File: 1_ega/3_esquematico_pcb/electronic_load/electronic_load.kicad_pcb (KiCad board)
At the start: 2 copper layers, 28 parts, among them J1 Encoder, J2 LCD_I2C, J3 GND, J4 MOS_GATE, J5 Isense, J6 Vload_LPF, J7 5V, Q1 IRF540N, SW1 BTN_MENU, SW2 BTN_STOP, U1 TL084

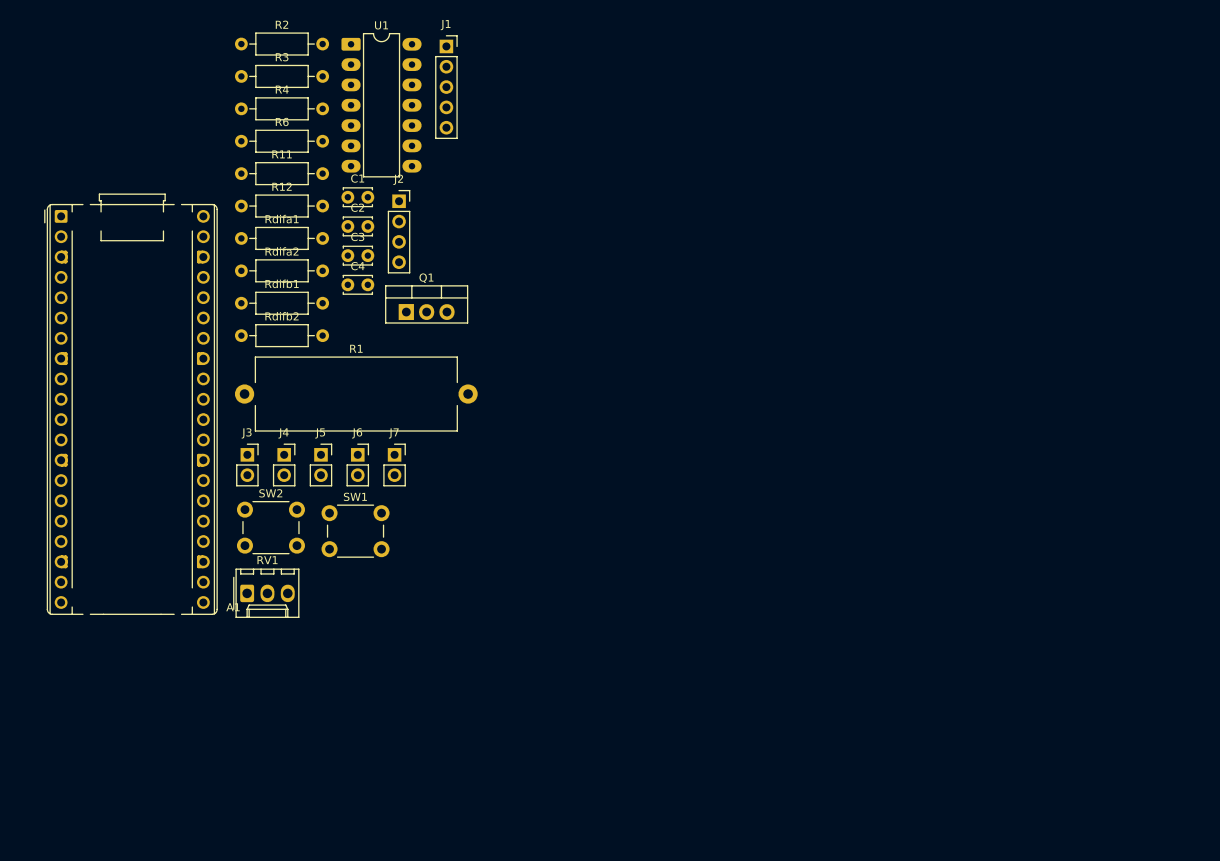
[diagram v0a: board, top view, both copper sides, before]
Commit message: test version of i2c_guard
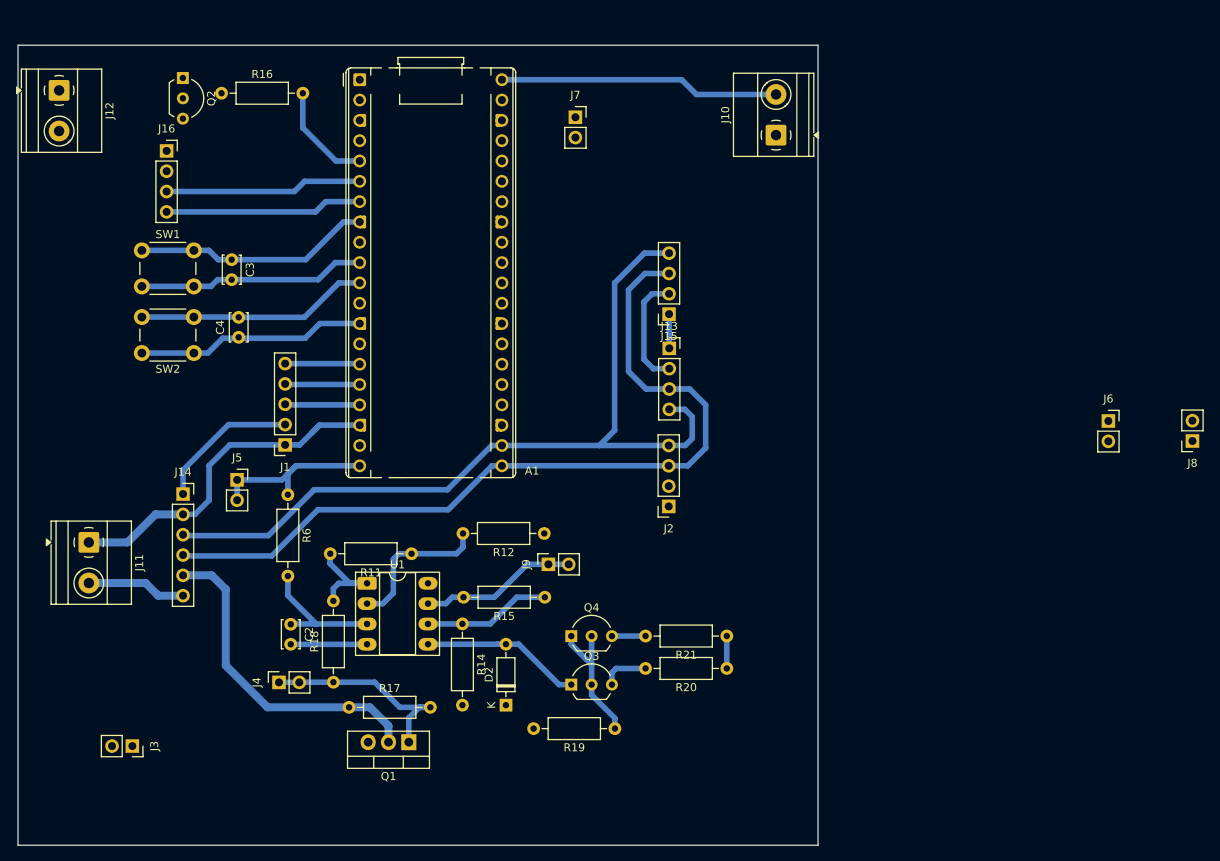
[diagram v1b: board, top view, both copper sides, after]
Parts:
- removed C1: 0.1uF, Capacitor_THT:C_Disc_D3.4mm_W2.1mm_P2.50mm
- removed R1: E100, Resistor_THT:R_Axial_Power_L25.0mm_W9.0mm_P27.94mm
- removed R2, R3, Rdifa1, Rdifa2, Rdifb1, Rdifb2: R, Resistor_THT:R_Axial_DIN0207_L6.3mm_D2.5mm_P10.16mm_Horizontal
- removed R4: 4.7k, Resistor_THT:R_Axial_DIN0207_L6.3mm_D2.5mm_P10.16mm_Horizontal
- removed RV1: Rdif_adj, Connector_Molex:Molex_KK-254_AE-6410-03A_1x03_P2.54mm_Vertical
- added D2: 1N4148, Diode_THT:D_DO-35_SOD27_P7.62mm_Horizontal, F.Cu at (81.0, 102.5)
- added J10: VCC, TerminalBlock_Phoenix:TerminalBlock_Phoenix_MKDS-1,5-2-5.08_1x02_P5.08mm_Horizontal, F.Cu at (114.8, 31.2)
- added J11: LOAD, TerminalBlock_Phoenix:TerminalBlock_Phoenix_MKDS-1,5-2-5.08_1x02_P5.08mm_Horizontal, F.Cu at (28.9, 82.1)
- added J12: FAN, TerminalBlock_Phoenix:TerminalBlock_Phoenix_MKDS-1,5-2-5.08_1x02_P5.08mm_Horizontal, F.Cu at (25.1, 25.6)
- added J13: RTC_I2C, Connector_PinSocket_2.54mm:PinSocket_1x04_P2.54mm_Vertical, F.Cu at (101.4, 57.9)
- added J14: INA219, Connector_PinSocket_2.54mm:PinSocket_1x06_P2.54mm_Vertical, F.Cu at (40.6, 76.1)
- added J15: EGB_I2C, Connector_PinSocket_2.54mm:PinSocket_1x04_P2.54mm_Vertical, F.Cu at (101.4, 53.6)
- added J16: EGB_UART, Connector_PinSocket_2.54mm:PinSocket_1x04_P2.54mm_Vertical, F.Cu at (38.6, 33.2)
- added J8: MOS_LPF, Connector_PinSocket_2.54mm:PinSocket_1x02_P2.54mm_Vertical, F.Cu at (166.8, 69.5)
- added J9: TEMP_DIODE, Connector_PinSocket_2.54mm:PinSocket_1x02_P2.54mm_Vertical, F.Cu at (86.3, 84.9)
- added Q2: 2n2222, Package_TO_SOT_THT:TO-92L_Inline_Wide, F.Cu at (40.6, 24.1)
- added Q3: BC327, Package_TO_SOT_THT:TO-92_Inline_Wide, F.Cu at (89.2, 99.9)
- added Q4: BC327, Package_TO_SOT_THT:TO-92_Inline_Wide, F.Cu at (89.2, 93.9)
- added R14: 5k1, Resistor_THT:R_Axial_DIN0207_L6.3mm_D2.5mm_P10.16mm_Horizontal, F.Cu at (75.5, 92.3)
- added R15: 1k, Resistor_THT:R_Axial_DIN0207_L6.3mm_D2.5mm_P10.16mm_Horizontal, F.Cu at (85.8, 89.0)
- added R16: 1.5k, Resistor_THT:R_Axial_DIN0207_L6.3mm_D2.5mm_P10.16mm_Horizontal, F.Cu at (45.4, 26.0)
- added R17: 10k, Resistor_THT:R_Axial_DIN0207_L6.3mm_D2.5mm_P10.16mm_Horizontal, F.Cu at (61.4, 102.8)
- added R18: 10R, Resistor_THT:R_Axial_DIN0207_L6.3mm_D2.5mm_P10.16mm_Horizontal, F.Cu at (59.4, 99.6)
- added R19: 5.1k, Resistor_THT:R_Axial_DIN0207_L6.3mm_D2.5mm_P10.16mm_Horizontal, F.Cu at (94.6, 105.4)
- added R20: 22k, Resistor_THT:R_Axial_DIN0207_L6.3mm_D2.5mm_P10.16mm_Horizontal, F.Cu at (108.6, 97.9)
- added R21: 22k, Resistor_THT:R_Axial_DIN0207_L6.3mm_D2.5mm_P10.16mm_Horizontal, F.Cu at (108.6, 93.9)
- J5: value Isense -> MOS_PWM
- R11: value R -> 51k
- R12: value R -> 20k
- U1: value TL084 -> LM358; footprint Package_DIP:DIP-14_W7.62mm_LongPads -> Package_DIP:DIP-8_W7.62mm_Socket_LongPads
- moved J6 93.9 mm to (156.3, 67.0)
- moved U1 67.4 mm to (63.6, 87.3)
- moved R12 55.8 mm to (85.8, 81.0), turned to 180 degrees
- moved Q1 53.8 mm to (68.8, 107.1), turned to 180 degrees
- moved J1 53.7 mm to (53.4, 70.0), turned to 180 degrees
- moved R11 52.1 mm to (69.2, 83.6), turned to 180 degrees
- moved J2 50.9 mm to (101.3, 77.7), turned to 180 degrees
- moved C2 50.2 mm to (54.1, 92.4), turned to -90 degrees
- moved J7 47.9 mm to (89.7, 29.0)
- moved R6 44.6 mm to (53.7, 76.2), turned to -90 degrees
- moved A1 41.0 mm to (62.7, 24.3)
- moved SW1 40.4 mm to (35.5, 45.6)
- moved J3 39.1 mm to (34.3, 107.6), turned to -90 degrees
- moved J4 28.5 mm to (52.6, 99.6), turned to 90 degrees
- moved SW2 20.6 mm to (42.0, 58.5), turned to 180 degrees
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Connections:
- A1 pad 13: LOAD- -> GND
- A1 pad 18: LOAD- -> GND
- A1 pad 20: unconnected-(A1-GPIO15-Pad20) -> MOS_PWM
- A1 pad 23: LOAD- -> GND
- A1 pad 24: MOS_PWM -> unconnected-(A1-GPIO18-Pad24)
- A1 pad 28: LOAD- -> GND
- A1 pad 3: LOAD- -> GND
- A1 pad 31: Isense -> TEMP_DIODE
- A1 pad 32: Vload_LPF -> unconnected-(A1-GPIO27_ADC1-Pad32)
- A1 pad 33: LOAD- -> unconnected-(A1-AGND-Pad33)
- A1 pad 38: LOAD- -> GND
- A1 pad 5: unconnected-(A1-GPIO3-Pad5) -> FAN_PWM
- A1 pad 6: unconnected-(A1-GPIO4-Pad6) -> TX_EGB
- A1 pad 7: unconnected-(A1-GPIO5-Pad7) -> RX_EGB
- A1 pad 8: LOAD- -> GND
- C2 pad 1: Net-(U1C-+) -> Net-(U1A-+)
- C2 pad 2: LOAD- -> GND
- C3 pad 1: LOAD- -> GND
- C4 pad 1: LOAD- -> GND
- J1 pad 1: LOAD- -> GND
- J2 pad 1: LOAD- -> GND
- J3 pad 1: LOAD- -> GND
- J3 pad 2: LOAD- -> GND
- J5 pad 1: Isense -> MOS_PWM
- J5 pad 2: Isense -> MOS_PWM
- J6 pad 1: Vload_LPF -> Net-(J6-Pin_1)
- J6 pad 2: Vload_LPF -> Net-(J6-Pin_1)
- Q1 pad 2: LOAD+ -> MOS_DRAIN
- Q1 pad 3: R+ -> GND
- R11 pad 1: Net-(U1C--) -> Net-(U1A--)
- R11 pad 2: MOS_GATE -> Net-(R11-Pad2)
- R12 pad 1: LOAD- -> GND
- R12 pad 2: Net-(U1C--) -> Net-(U1A--)
- R6 pad 2: Net-(U1C-+) -> Net-(U1A-+)
- SW1 pad 1: LOAD- -> GND
- SW2 pad 1: LOAD- -> GND
- U1 pad 1: Isense -> Net-(R11-Pad2)
- U1 pad 4: VCC -> GND
- U1 pad 5: Vload -> Net-(D2-A)
- U1 pad 7: Net-(U1B--) -> TEMP_DIODE
- U1 pad 8: MOS_GATE -> VCC
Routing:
- net GND: track 0.00 -> 116.1 mm
- net I2C_SCL: track 0.00 -> 104.2 mm
- net I2C_SDA: track 0.00 -> 103.8 mm
- net MOS_DRAIN: track 0.00 -> 41.1 mm
- net +3V3: track 0.00 -> 36.5 mm
- net +5V: track 0.00 -> 35.0 mm
- net BTN_STOP: track 0.00 -> 29.0 mm
- net BTN_MENU: track 0.00 -> 28.5 mm
- net MOS_GATE: track 0.00 -> 26.5 mm
- net RX_EGB: track 0.00 -> 24.7 mm
- net TX_EGB: track 0.00 -> 24.7 mm
- net MOS_PWM: track 0.00 -> 22.6 mm
- net Net-(D2-A): track 0.00 -> 20.0 mm
- net TEMP_DIODE: track 0.00 -> 19.6 mm
- net Net-(U1A--): track 0.00 -> 19.1 mm
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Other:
- board outline added: 100 x 100 mm

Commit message: feat: schematic and pcb full v1
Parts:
- removed J12: FAN, TerminalBlock_Phoenix:TerminalBlock_Phoenix_MKDS-1,5-2-5.08_1x02_P5.08mm_Horizontal
- removed J13: RTC_I2C, Connector_PinSocket_2.54mm:PinSocket_1x04_P2.54mm_Vertical
- removed Q2: 2n2222, Package_TO_SOT_THT:TO-92L_Inline_Wide
- removed R16: 1.5k, Resistor_THT:R_Axial_DIN0207_L6.3mm_D2.5mm_P10.16mm_Horizontal
- added C1: 100uF, Capacitor_THT:CP_Radial_D6.3mm_P2.50mm, F.Cu at (105.6, 95.9)
- added C5: 10nF, Capacitor_THT:C_Disc_D3.4mm_W2.1mm_P2.50mm, F.Cu at (86.2, 116.7)
- added C6: 470uF, Capacitor_THT:CP_Radial_D6.3mm_P2.50mm, F.Cu at (60.4, 111.1)
- added D1: 1N5819, Diode_THT:D_DO-41_SOD81_P10.16mm_Horizontal, F.Cu at (68.5, 111.4)
- added G***: LOGO, LOGO, B.Cu at (28.9, 54.3)
- added J17: EGB_I2C, Connector_PinSocket_2.54mm:PinSocket_1x03_P2.54mm_Vertical, F.Cu at (39.9, 59.5)
- added J18: EGB_UART, Connector_PinSocket_2.54mm:PinSocket_1x03_P2.54mm_Vertical, F.Cu at (39.8, 36.9)
- added L1: 170uH, Inductor_THT:L_Radial_D10.5mm_P5.00mm_Abacron_AISR-01, F.Cu at (98.3, 109.7)
- added R22: 0.22R, Resistor_THT:R_Axial_DIN0207_L6.3mm_D2.5mm_P10.16mm_Horizontal, F.Cu at (88.5, 98.0)
- added R23: 200R, Resistor_THT:R_Axial_DIN0207_L6.3mm_D2.5mm_P10.16mm_Horizontal, F.Cu at (88.4, 102.1)
- added R24: 47k, Resistor_THT:R_Axial_DIN0207_L6.3mm_D2.5mm_P10.16mm_Horizontal, F.Cu at (78.5, 106.8)
- added R25: 3.3k, Resistor_THT:R_Axial_DIN0207_L6.3mm_D2.5mm_P10.16mm_Horizontal, F.Cu at (82.6, 104.7)
- added U2: MC34063AD, Package_SO:SOIC-8_3.9x4.9mm_P1.27mm, B.Cu at (89.3, 110.2)
- A1: footprint Module:RaspberryPi_Pico_Common_THT -> electronic_load:RaspberryPi_Pico_2_THT
- J1: footprint Connector_PinSocket_2.54mm:PinSocket_1x05_P2.54mm_Vertical -> Connector_PinHeader_2.54mm:PinHeader_1x05_P2.54mm_Vertical
- J10: value VCC -> 5V
- J14: footprint Connector_PinSocket_2.54mm:PinSocket_1x06_P2.54mm_Vertical -> electronic_load:INA219
- J15: value EGB_I2C -> VCC; footprint Connector_PinSocket_2.54mm:PinSocket_1x04_P2.54mm_Vertical -> TerminalBlock_Phoenix:TerminalBlock_Phoenix_MKDS-1,5-2-5.08_1x02_P5.08mm_Horizontal
- J16: value EGB_UART -> LCD_I2C; footprint Connector_PinSocket_2.54mm:PinSocket_1x04_P2.54mm_Vertical -> Connector_PinHeader_2.54mm:PinHeader_1x02_P2.54mm_Vertical
- J2: value LCD_I2C -> RTC_I2C; footprint Connector_PinSocket_2.54mm:PinSocket_1x04_P2.54mm_Vertical -> Connector_PinSocket_2.54mm:PinSocket_1x06_P2.54mm_Vertical
- J3, J4, J5, J9: footprint Connector_PinSocket_2.54mm:PinSocket_1x02_P2.54mm_Vertical -> Connector_PinHeader_2.54mm:PinHeader_1x02_P2.54mm_Vertical
- J6: value Vload_LPF -> LCD_PWR; footprint Connector_PinSocket_2.54mm:PinSocket_1x02_P2.54mm_Vertical -> Connector_PinHeader_2.54mm:PinHeader_1x02_P2.54mm_Vertical
- J7: value 5V -> GND; footprint Connector_PinSocket_2.54mm:PinSocket_1x02_P2.54mm_Vertical -> Connector_PinHeader_2.54mm:PinHeader_1x02_P2.54mm_Vertical
- J8: value MOS_LPF -> MOS_VDS; footprint Connector_PinSocket_2.54mm:PinSocket_1x02_P2.54mm_Vertical -> Connector_PinHeader_2.54mm:PinHeader_1x02_P2.54mm_Vertical
- R11: value 51k -> 20k
- R12: value 20k -> 5.1k
- R14: value 5k1 -> 5.1k
- R15: value 1k -> 20k
- SW1, SW2: footprint Button_Switch_THT:SW_PUSH_6mm -> Connector_PinHeader_2.54mm:PinHeader_1x02_P2.54mm_Vertical
- moved J15 81.6 mm to (46.3, 113.7), turned to 0 degrees
- moved J11 79.9 mm to (108.1, 72.0), turned to 90 degrees
- moved J8 78.8 mm to (89.9, 86.9), turned to 0 degrees
- moved J3 77.8 mm to (39.7, 30.0), turned to 180 degrees
- moved R21 75.0 mm to (34.7, 81.0), turned to -90 degrees
- moved J6 72.6 mm to (96.9, 25.2)
- moved R20 69.9 mm to (40.8, 81.0), turned to -90 degrees
- moved J16 65.4 mm to (94.0, 67.9), turned to 90 degrees
- moved R19 61.9 mm to (32.8, 104.2), turned to 0 degrees
- moved Q4 54.8 mm to (34.7, 99.6), turned to 90 degrees
- moved J14 50.7 mm to (88.9, 60.6), turned to 90 degrees
- moved Q3 48.3 mm to (40.8, 99.6), turned to 90 degrees
- moved J4 41.1 mm to (89.9, 82.3), turned to 180 degrees
- moved J2 41.1 mm to (93.1, 37.4), turned to -90 degrees
- moved Q1 39.5 mm to (99.9, 82.7), turned to -90 degrees
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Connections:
- A1 pad 10: BTN_MENU -> BTN_STOP
- A1 pad 11: BTN_STOP -> unconnected-(A1-GPIO8-Pad11)
- A1 pad 14: unconnected-(A1-GPIO10-Pad14) -> I2C1_SCL
- A1 pad 15: ENC_CLK -> I2C1_SDA
- A1 pad 16: ENC_DT -> ENC_CLK
- A1 pad 17: ENC_SW -> ENC_DT
- A1 pad 19: unconnected-(A1-GPIO14-Pad19) -> ENC_SW
- A1 pad 20: MOS_PWM -> unconnected-(A1-GPIO15-Pad20)
- A1 pad 24: unconnected-(A1-GPIO18-Pad24) -> MOS_PWM
- A1 pad 5: FAN_PWM -> unconnected-(A1-GPIO3-Pad5)
- A1 pad 9: unconnected-(A1-GPIO6-Pad9) -> BTN_MENU
- C2 pad 1: Net-(U1A-+) -> Net-(U1B-+)
- J15 pad 2: +3V3 -> VCC
- J16 pad 1: GND -> I2C_SCL
- J16 pad 2: +3V3 -> I2C_SDA
- J2 pad 1: GND -> RTC_32K
- J2 pad 2: +5V -> RTC_SQW
- J2 pad 3: I2C_SDA -> I2C_SCL
- J2 pad 4: I2C_SCL -> I2C_SDA
- J6 pad 1: Net-(J6-Pin_1) -> +5V
- J6 pad 2: Net-(J6-Pin_1) -> GND
- J7 pad 1: +5V -> GND
- J7 pad 2: +5V -> GND
- J8 pad 1: Net-(J8-Pin_1) -> MOS_DRAIN
- J8 pad 2: Net-(J8-Pin_1) -> MOS_DRAIN
- R11 pad 1: Net-(U1A--) -> Net-(U1B--)
- R12 pad 2: Net-(U1A--) -> Net-(U1B--)
- R14 pad 1: Net-(U1B--) -> Net-(U1A--)
- R15 pad 1: Net-(U1B--) -> Net-(U1A--)
- R6 pad 2: Net-(U1A-+) -> Net-(U1B-+)
- U1 pad 1: Net-(R11-Pad2) -> TEMP_DIODE
- U1 pad 3: Net-(U1A-+) -> Net-(D2-A)
- U1 pad 5: Net-(D2-A) -> Net-(U1B-+)
- U1 pad 7: TEMP_DIODE -> Net-(R11-Pad2)
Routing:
- net GND: track 116.1 -> 363.2 mm
- net +5V: track 35.0 -> 149.4 mm
- net +3V3: track 36.5 -> 124.1 mm
- net VCC: track 0.00 -> 47.3 mm
- net I2C_SCL: track 104.2 -> 57.0 mm
- net TEMP_DIODE: track 19.6 -> 63.5 mm
- net Net-(U2-Ipk): track 0.00 -> 34.6 mm
- net I2C_SDA: track 103.8 -> 75.3 mm
- net Net-(D1-A): track 0.00 -> 23.4 mm
- net Net-(U1A-+): track 17.0 -> 0.00 mm
- net I2C1_SDA: track 0.00 -> 15.6 mm
- net I2C1_SCL: track 0.00 -> 15.6 mm
- net Net-(U1B-+): track 0.00 -> 14.8 mm
- net FAN_PWM: track 13.2 -> 0.00 mm
- net BTN_MENU: track 28.5 -> 15.3 mm
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- added copper zone on B.Cu, net GND
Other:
- board text added: "TD III 2025 - Pablo Gomez - Nico"
